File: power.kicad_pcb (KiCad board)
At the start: 2 copper layers, 23 parts, among them J1 USB_C_Receptacle, J2 AVR-ISP-6, U1 INA226, U2 AMS1117-3.3, U3 ATmega328P-A, Y1 Crystal

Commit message: PCB Routing Starting
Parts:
- removed DS1: OLED-128O064D, Display:OLED-128O064D
- removed R8: 4.7kΩ, Resistor_SMD:R_0603_1608Metric
- C6: value 1µF -> 0.1 µF
- moved J1 49.9 mm to (110.5, 69.5), turned to -90 degrees
- moved U3 47.2 mm to (175.5, 57.5)
- moved U2 30.8 mm to (176.0, 69.0)
- moved C6 30.7 mm to (129.3, 51.5)
- moved U1 30.1 mm to (177.3, 78.5)
- moved R1 28.0 mm to (172.0, 79.0)
- moved R2 27.2 mm to (172.0, 80.6)
- moved Y1 23.8 mm to (166.9, 63.7)
- moved R6 21.4 mm to (176.0, 51.5)
- moved R7 18.8 mm to (169.7, 71.5)
- moved R9 10.9 mm to (172.7, 51.5)
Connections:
- Brd1 pad 1: unconnected-(Brd1-GND-Pad1) -> GND
- Brd1 pad 2: unconnected-(Brd1-VCC-Pad2) -> 3V3
- Brd1 pad 3: unconnected-(Brd1-SCL-Pad3) -> SCL
- Brd1 pad 4: unconnected-(Brd1-SDA-Pad4) -> SDA
- C6 pad 1: GND -> 3V3
- C6 pad 2: 3V3 -> GND
- U3 pad 1: D3 -> unconnected-(U3-PD3-Pad1)
- U3 pad 10: D6 -> unconnected-(U3-PD6-Pad10)
- U3 pad 11: D7 -> unconnected-(U3-PD7-Pad11)
- U3 pad 12: OLED_RESET -> unconnected-(U3-PB0-Pad12)
- U3 pad 13: D/C -> unconnected-(U3-PB1-Pad13)
- U3 pad 14: R/W -> unconnected-(U3-PB2-Pad14)
- U3 pad 2: D4 -> unconnected-(U3-PD4-Pad2)
- U3 pad 23: E/RD -> unconnected-(U3-PC0-Pad23)
- U3 pad 30: D0 -> unconnected-(U3-PD0-Pad30)
- U3 pad 31: D1 -> unconnected-(U3-PD1-Pad31)
- U3 pad 32: D2 -> unconnected-(U3-PD2-Pad32)
- U3 pad 9: D5 -> unconnected-(U3-PD5-Pad9)
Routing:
- net GND: track 0.00 -> 1.77 mm
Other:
- board outline added: 72.5 x 40 mm

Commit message: Schematic 95% done
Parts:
- moved R4 45.0 mm to (116.3, 70.3), turned to -90 degrees
- moved R3 44.9 mm to (116.3, 67.2), turned to -90 degrees
- moved C5 44.3 mm to (112.0, 63.0), turned to 180 degrees
- moved J2 27.3 mm to (159.2, 53.4)
- moved C1 24.2 mm to (159.7, 77.5)
- moved C2 24.1 mm to (172.0, 74.3), turned to 90 degrees
- moved C4 12.0 mm to (163.7, 70.5)
- moved R5 12.0 mm to (170.7, 57.5)
- moved U2 11.2 mm to (166.5, 75.0)
- moved Y1 10.4 mm to (158.4, 69.7)
- moved R1 10.4 mm to (163.5, 85.0), turned to 180 degrees
- moved R2 10.4 mm to (163.5, 86.6)
- moved R6 10.4 mm to (167.5, 57.5)
- moved R9 10.4 mm to (164.2, 57.5)
- moved U1 10.4 mm to (168.8, 84.5)
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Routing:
- net 3V3: track 0.00 -> 138.1 mm
- net SCL: track 0.00 -> 82.4 mm, vias 0 -> 5
- net SDA: track 0.00 -> 74.8 mm, vias 0 -> 2
- net VBUS: track 0.00 -> 71.4 mm, vias 0 -> 3
- net GND: track 1.77 -> 62.0 mm, vias 0 -> 9
- net MOSI: track 0.00 -> 40.4 mm, vias 0 -> 2
- net MISO: track 0.00 -> 30.3 mm, vias 0 -> 2
- net Net-(J1-SHIELD): track 0.00 -> 19.3 mm
- net SCK: track 0.00 -> 19.3 mm, vias 0 -> 2
- net INPUT_PW: track 0.00 -> 16.7 mm
- net Net-(U3-XTAL2/PB7): track 0.00 -> 14.9 mm
- net RESET: track 0.00 -> 10.9 mm, vias 0 -> 2
- net Net-(U3-XTAL1/PB6): track 0.00 -> 9.04 mm
- net Net-(J1-CC2): track 0.00 -> 6.60 mm
- net Net-(J1-CC1): track 0.00 -> 3.74 mm
- added copper zone on B.Cu, net GND
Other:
- board size 72.5 x 40 mm -> 66.2 x 40 mm

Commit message: Small DRC Fixes
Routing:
- net VBUS: track 71.4 -> 70.6 mm
- net SCL: vias 5 -> 4
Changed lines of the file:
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@@
 		(tags "resistor")
 		(property "Reference" "R7"
-			(at 0 -1.43 0)
+			(at 1 -1.25 0)
 			(layer "F.SilkS")
 			(effects
@@
 			(unlocked yes)
 			(layer "F.SilkS")
+			(hide yes)
 			(effects
 				(font
@@
 			)
 		)
-		(property "Datasheet" "https://www.usb.org/sites/default/files/documents/usb_type-c.zip"
+		(property "Datasheet" ""
 			(at 0 1.575 270)
 			(unlocked yes)
@@
 			)
 		)
-		(property "Description" "USB Full-Featured Type-C Receptacle connector"
+		(property "Description" ""
 			(at 0 1.575 270)
 			(unlocked yes)
@@
 		(tags "resistor")
 		(property "Reference" "R2"
-			(at 0 -1.43 0)
+			(at -2.490411 -1.554819 0)
 			(layer "F.SilkS")
 			(effects
@@
 		(tags "capacitor")
 		(property "Reference" "C5"
-			(at 0 -1.43 0)
+			(at 2 0 90)
 			(layer "F.SilkS")
 			(effects
@@
 		(tags "Adafruit SSD1306 OLED 1.3 inch 128x64 I2C & SPI ")
 		(property "Reference" "Brd1"
-			(at 8.89 -5 0)
+			(at -2.61 -4.085 0)
 			(layer "F.SilkS")
 			(effects
@@
 		(tags "TQFP QFP")
 		(property "Reference" "U3"
-			(at 0 -5.85 0)
+			(at 4.319711 -4.401571 0)
 			(layer "F.SilkS")
 			(effects
@@
 		(tags "capacitor")
 		(property "Reference" "C6"
-			(at 0 -1.43 0)
+			(at -2.475 -0.5 0)
 			(layer "F.SilkS")
 			(effects
@@
 		(tags "resistor")
 		(property "Reference" "R1"
-			(at 0 -1.43 0)
+			(at 2.5 -1.492947 0)
 			(layer "F.SilkS")
 			(effects
@@
 		(tags "resistor")
 		(property "Reference" "R4"
-			(at 0 -1.43 90)
+			(at 2.7083 -0.203335 90)
 			(layer "F.SilkS")
 			(effects
@@
 		(tags "capacitor")
 		(property "Reference" "C2"
-			(at 0 -1.43 90)
+			(at 2.275 -2.25 90)
 			(layer "F.SilkS")
 			(effects
@@
 	)
 	(via
-		(at 160 60.5)
-		(size 0.6)
-		(drill 0.3)
-		(layers "F.Cu" "B.Cu")
-		(net 4)
-	)
-	(via
 		(at 162.5 88.5)
 		(size 0.6)
@@
 	)
 	(segment
-		(start 171 83.5)
-		(end 169.5 83.5)
+		(start 167.675 81.675)
+		(end 167.675 80.5)
 		(width 0.2)
 		(layer "F.Cu")
@@
 	)
 	(segment
-		(start 167.675 81.675)
-		(end 167.675 80.5)
+		(start 171 83.5)
+		(end 169.5 83.5)
+		(width 0.2)
+		(layer "F.Cu")
+		(net 8)
+	)
+	(segment
+		(start 169.5 83.5)
+		(end 167.675 81.675)
 		(width 0.2)
 		(layer "F.Cu")
@@
 		(width 0.2)
 		(layer "F.Cu")
-		(net 8)
-	)
-	(segment
-		(start 167.675 81.325)
-		(end 167.675 80.5)
-		(width 0.2)
-		(layer "F.Cu")
-		(net 8)
-	)
-	(segment
-		(start 169.5 83.5)
-		(end 167.675 81.675)
-		(width 0.2)
-		(layer "F.Cu")

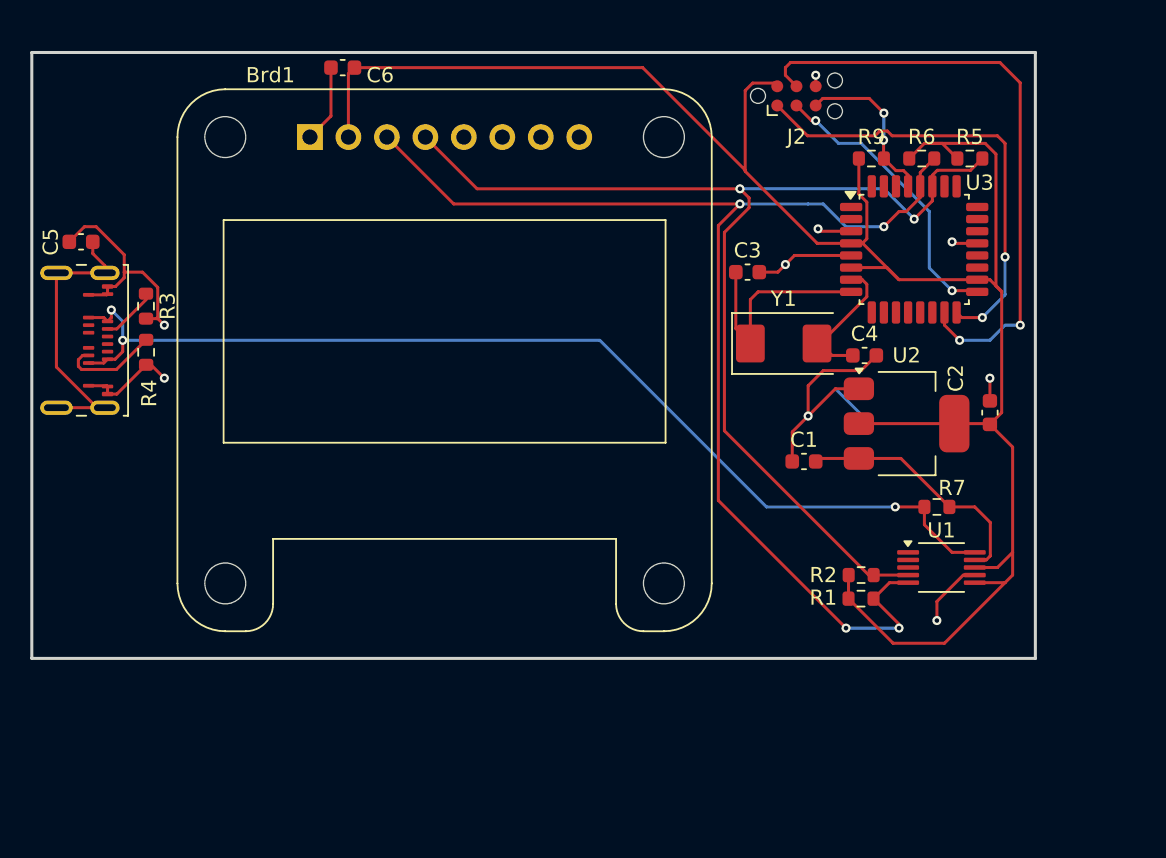
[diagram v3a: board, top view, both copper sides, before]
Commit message: Switched to 5V over 3.3V for MCU for programming
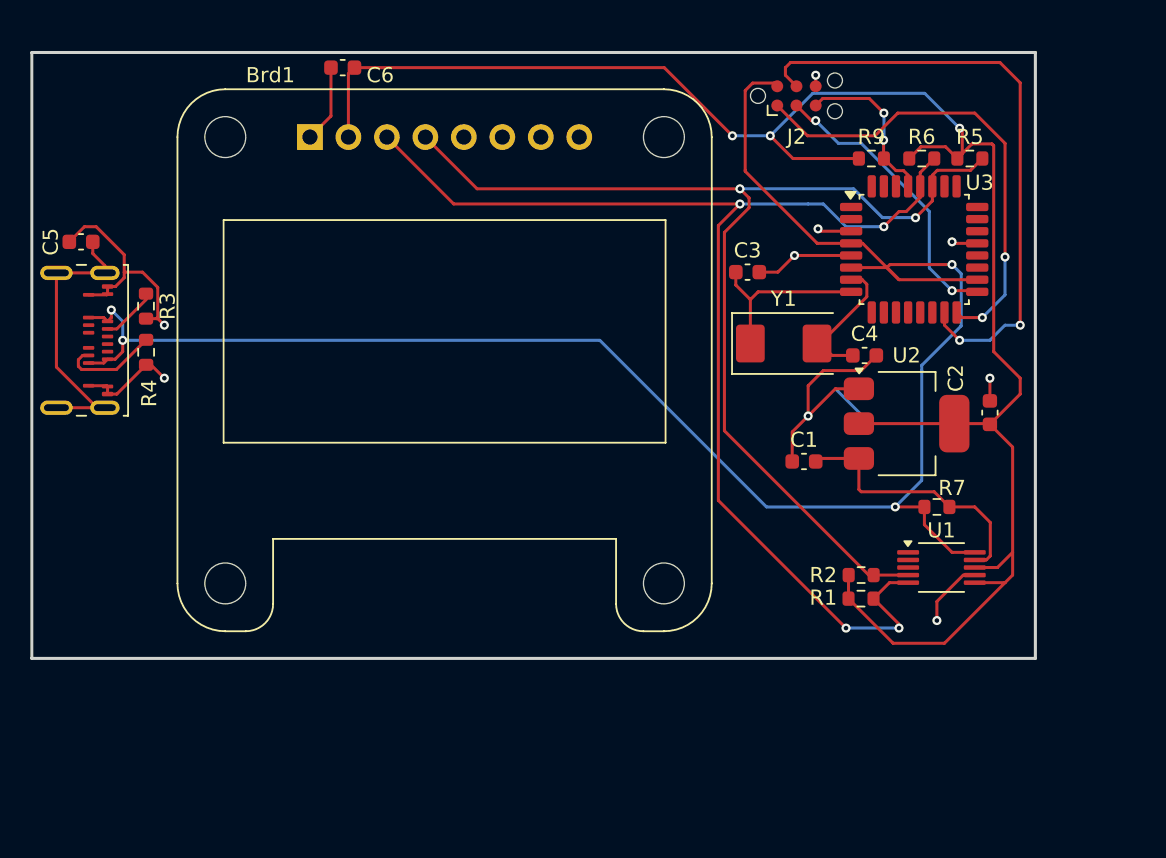
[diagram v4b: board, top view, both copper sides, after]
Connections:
- J2 pad 2: 3V3 -> VBUS
- U3 pad 18: 3V3 -> VBUS
- U3 pad 4: 3V3 -> VBUS
- U3 pad 6: 3V3 -> VBUS
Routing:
- net VBUS: track 70.6 -> 123.3 mm, vias 3 -> 4
- net 3V3: track 138.1 -> 123.6 mm, vias 0 -> 3
- net Net-(U3-XTAL2/PB7): track 14.9 -> 12.0 mm
- net INPUT_PW: track 16.7 -> 17.9 mm
- net MISO: track 30.3 -> 31.3 mm

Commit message: Small PCB changes
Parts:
- added G***: LOGO, LOGO, B.Cu at (144.5, 69.0)
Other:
- board text added: "By: Scooter"

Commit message: Finished it all!
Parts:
- J2: footprint Connector:Tag-Connect_TC2030-IDC-NL_2x03_P1.27mm_Vertical -> Connector_PinHeader_1.27mm:PinHeader_2x03_P1.27mm_Vertical
- Y1: footprint Crystal:Crystal_SMD_0603-2Pin_6.0x3.5mm -> Crystal:Crystal_SMD_Abracon_ABM3-2Pin_5.0x3.2mm
- moved J2 1.29 mm to (158.0, 53.8), turned to 90 degrees
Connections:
- U1 pad 1: unconnected-(U1-A1-Pad1) -> GND
- U1 pad 2: unconnected-(U1-A0-Pad2) -> GND
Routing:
- net GND: track 62.0 -> 68.4 mm
- net 3V3: track 123.6 -> 129.7 mm
- added copper zone on F.Cu, net GND
